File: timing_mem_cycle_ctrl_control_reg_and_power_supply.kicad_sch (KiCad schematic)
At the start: 59 parts, among them U10 LS175, U11 LS20, U20 LS10, U21 LS161, U30 LS20, U31 LS00, U32 LS109, U4 LS04, U42 LS109, U5 LS109, U50 LS368, U52 LS00, U57 LS13, U60 7406, U62 LS08

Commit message: First version of the schematic completed
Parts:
- U10: symbol 74LS175:74LS175_U10 -> LS_Logic:74LS175_U10
- U11: symbol 74LS20:74LS20_U11 -> LS_Logic:74LS20_U11
- U20: symbol 74LS10:74LS10_U20 -> LS_Logic:74LS10_U20
- U21: symbol 74LS161:74LS161_U21 -> LS_Logic:74LS161_U21
- U4: footprint Package_DIP:DIP-14_W7.62mm_LongPads -> (none)
- U50: symbol 74LS368:74LS368_U50 -> LS_Logic:74LS368_U50_U59
- U57: symbol 74xx:74LS13 -> LS_Logic:74LS13_U57
- renumbered C1000 to C101
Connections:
- net +5V: now also VR2.3 (OUT); no longer VR2.1 (IN)
- net 6502_+7.5V: now also VR2.1 (IN); no longer VR2.3 (OUT)
- net CNTC: no longer JP1.3 (C), U11.9, U21.11 (Q3), U5.12 (C)
- net MEM_CYC_ENAB renamed MEM_CYC_ENABLE
- net SYST_RAM_ADDR renamed SYST_RAM_ADRD
- net USR_RAM_ADDR renamed USER_RAM_ADRD
- net ~{MEM_MODE} renamed ~{MFM_MODE}
- new net: JP1.3 (C), U11.9, U21.11 (Q3), U5.12 (C)
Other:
- moved on the sheet: VR2

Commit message: Schematic corrections
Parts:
- C10, C11, C8: footprint (none) -> K_1013_Jumper:CP_Radial_D8.0mm_P5.08mm
- C7: footprint (none) -> K_1013_Jumper:CP_Axial_L30.0mm_D12.5mm_P36.83mm_Horizontal
- C88, C89, C9, C98, C99: footprint (none) -> K_1013_Jumper:C_Disc_D7.0mm_W2.5mm_P6.35mm
- D1, D2, D3: footprint (none) -> K_1013_Jumper:D_DO-35_SOD27_P12.70mm_Horizontal
- R11: footprint Resistor_THT:R_Axial_DIN0207_L6.3mm_D2.5mm_P10.16mm_Horizontal -> K_1013_Jumper:R_Axial_DIN0309_L9.0mm_D3.2mm_P12.70mm_Horizontal
- R11: footprint Resistor_THT:R_Axial_DIN0207_L6.3mm_D2.5mm_P10.16mm_Horizontal -> K_1013_Jumper:R_Axial_DIN0204_L3.6mm_D2.5mm_P12.70mm_Horizontal
- R27: footprint (none) -> K_1013_Jumper:Potentiometer_Bourns_3339P_Vertical
- TP1: footprint (none) -> K_1013_Jumper:TestPoint_1.8
- TP11, TP13, TP5, TP6: footprint (none) -> K_1013_Jumper:TestPoint
- TP2: footprint (none) -> K_1013_Jumper:TestPoint_2.4
- TP3, TP7: footprint (none) -> K_1013_Jumper:TestPoint_3.0
- U10, U21, U32, U42, U5, U50: footprint (none) -> K_1013_Jumper:DIP-16_W7.62mm_LongPads
- U11, U30, U4: footprint Package_DIP:DIP-14_W7.62mm_LongPads -> K_1013_Jumper:DIP-14_W7.62mm_LongPads
- U20, U31, U4, U52, U57, U60, U62: footprint (none) -> K_1013_Jumper:DIP-14_W7.62mm_LongPads
- VR1: footprint (none) -> K_1013_Jumper:TO-202-3_Horizontal_TabDown
- VR2: footprint (none) -> K_1013_Jumper:TO-220-3_Horizontal_TabDown

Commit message: Update progress
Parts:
- C10, C11, C8: footprint K_1013_Jumper:CP_Radial_D8.0mm_P5.08mm -> K_1013:CP_Radial_D8.0mm_P5.08mm
- C7: footprint K_1013_Jumper:CP_Axial_L30.0mm_D12.5mm_P36.83mm_Horizontal -> K_1013:CP_Axial_L30.0mm_D12.5mm_P35.56mm_Horizontal
- C88, C89, C9, C98, C99: footprint K_1013_Jumper:C_Disc_D7.0mm_W2.5mm_P6.35mm -> K_1013:C_Disc_D7.0mm_W2.5mm_P6.35mm
- D1, D2, D3: footprint K_1013_Jumper:D_DO-35_SOD27_P12.70mm_Horizontal -> K_1013:D_DO-35_SOD27_P12.70mm_Horizontal
- JP1: footprint K_1013_Jumper:Jumper-4 -> K_1013:Jumper-4
- R13, R14, R5, R6: renamed from R11; footprint K_1013_Jumper:R_Axial_DIN0204_L3.6mm_D2.5mm_P12.70mm_Horizontal -> K_1013:R_Axial_DIN0204_L3.6mm_D2.5mm_P12.70mm_Horizontal
- R22, R28, R29, R30, R31, R53, R54, R55: renamed from R11; footprint K_1013_Jumper:R_Axial_DIN0309_L9.0mm_D3.2mm_P12.70mm_Horizontal -> K_1013:R_Axial_DIN0309_L9.0mm_D3.2mm_P12.70mm_Horizontal
- R27: footprint K_1013_Jumper:Potentiometer_Bourns_3339P_Vertical -> K_1013:Potentiometer_Bourns_3339P_Vertical
- TP1: footprint K_1013_Jumper:TestPoint_1.8 -> K_1013:TestPoint_1.8
- TP11, TP13, TP5, TP6: footprint K_1013_Jumper:TestPoint -> K_1013:TestPoint
- TP2: footprint K_1013_Jumper:TestPoint_2.4 -> K_1013:TestPoint_2.4
- TP3, TP7: footprint K_1013_Jumper:TestPoint_3.0 -> K_1013:TestPoint_3.0
- U10, U21, U32, U42, U5, U50: footprint K_1013_Jumper:DIP-16_W7.62mm_LongPads -> K_1013:DIP-16_W7.62mm_LongPads
- U11, U20, U30, U31, U4, U52, U57, U60, U62: footprint K_1013_Jumper:DIP-14_W7.62mm_LongPads -> K_1013:DIP-14_W7.62mm_LongPads
- U19: renamed from U4; footprint K_1013_Jumper:DIP-14_W7.62mm_LongPads -> K_1013:DIP-14_W7.62mm_LongPads_U19
- U51, U53: renamed from U4; footprint K_1013_Jumper:DIP-14_W7.62mm_LongPads -> K_1013:DIP-14_W7.62mm_LongPads
- VR1: footprint K_1013_Jumper:TO-202-3_Horizontal_TabDown -> K_1013:TO-202-3_Horizontal_TabDown
- VR2: footprint K_1013_Jumper:TO-220-3_Horizontal_TabDown -> K_1013:TO-220-3_Horizontal_TabDown
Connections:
- net 6502_+7.5V: now also C11.1; no longer C11.2
- net 6502_Ø2: now also U4.5; no longer U4.1
- net 8MHZ_CLOCK: now also U51.4; no longer U51.2
- net CNTB: now also U4.9; no longer U4.1
- net DMA_CYC: now also U53.12; no longer U53.2
- net FDC_WRT_CLK: now also U4.12; no longer U4.2
- net GND: now also C11.2; no longer C11.1
- net LOC_~{R}/W: now also U30.2; no longer U30.10
- net LOC_Ø2: now also U19.12; no longer U19.2
- net REF_CYC: now also U4.10; no longer U4.2
- net SYST_RAM_ADRD: now also U30.1; no longer U30.9
- net ~{CNTC}: now also U30.4; no longer U30.12
- net ~{DMA_CYC}: now also U53.13; no longer U53.1
- net ~{LOC_Ø2}: now also U19.13, U4.6; no longer U19.1, U4.2
- net ~{REF_CYC}: now also U4.11; no longer U4.1
- net at U20.10, U31.5: now also U4.8; no longer U4.2
- net at R27.2, R27.3, U21.2 (CP)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: now also U51.3; no longer U51.1
- net at U11.6: now also U4.13; no longer U4.1
- net at U10.6 (~{Q1}): now also U30.5; no longer U30.13
- net at U20.13: now also U30.6; no longer U30.8
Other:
- moved on the sheet: C11

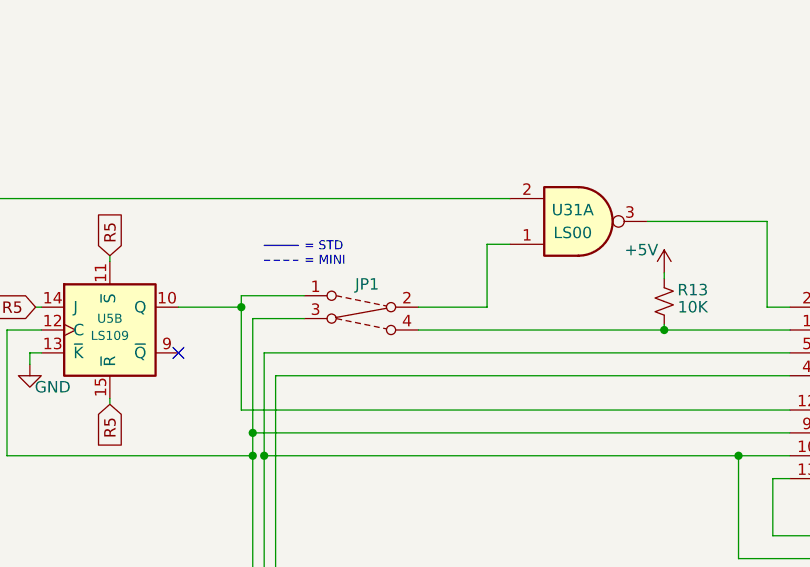
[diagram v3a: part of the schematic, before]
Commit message: Routing of the bottom layer completed
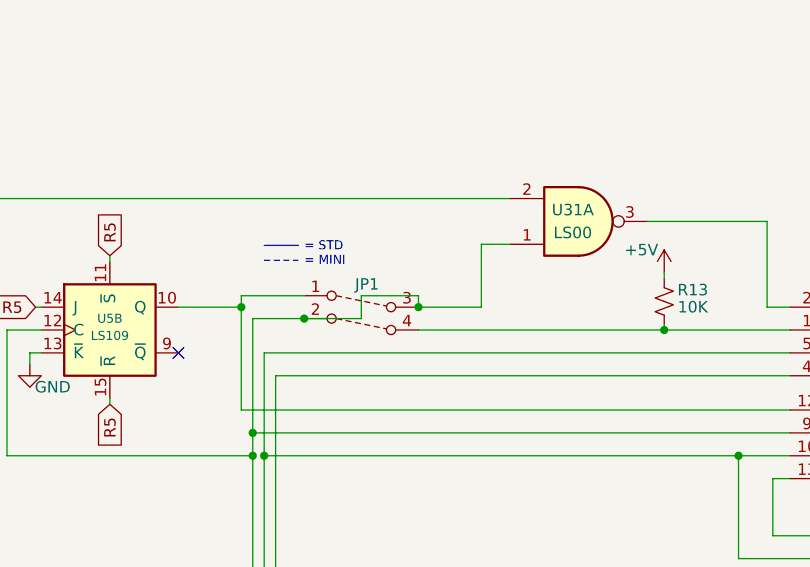
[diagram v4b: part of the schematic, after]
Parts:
- U21: footprint K_1013:DIP-16_W7.62mm_LongPads -> K_1013:DIP-16_W7.62mm_LongPads_U21
- U30: footprint K_1013:DIP-14_W7.62mm_LongPads -> K_1013:DIP-14_W7.62mm_LongPads_U30
- U31: footprint K_1013:DIP-14_W7.62mm_LongPads -> K_1013:DIP-14_W7.62mm_LongPads_U31
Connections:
- net at JP1.3, U11.9, U21.11 (Q3)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: now also JP1.2, U31.1
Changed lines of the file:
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@@
   (junction (at 341.63 210.185) (diameter 0) (color 0 0 0 0)
   )
+  (junction (at 86.995 59.69) (diameter 0) (color 0 0 0 0)
+  )
   (junction (at 80.645 200.025) (diameter 0) (color 0 0 0 0)
   )
@@
   (junction (at 351.79 151.765) (diameter 0) (color 0 0 0 0)
   )
+  (junction (at 81.28 74.93) (diameter 0) (color 0 0 0 0)
+  )
   (junction (at 369.57 160.655) (diameter 0) (color 0 0 0 0)
   )
@@
   (junction (at 235.585 86.36) (diameter 0) (color 0 0 0 0)
   )
-  (junction (at 81.28 72.39) (diameter 0) (color 0 0 0 0)
-  )
   (junction (at 370.205 198.12) (diameter 0) (color 0 0 0 0)
   )
@@
   (junction (at 280.67 97.155) (diameter 0) (color 0 0 0 0)
   )
-  (junction (at 81.28 74.93) (diameter 0) (color 0 0 0 0)
-  )
   (junction (at 341.63 198.12) (diameter 0) (color 0 0 0 0)
   )
@@
   (junction (at 299.72 198.12) (diameter 0) (color 0 0 0 0)
   )
+  (junction (at 81.28 72.39) (diameter 0) (color 0 0 0 0)
+  )
   (junction (at 321.31 210.185) (diameter 0) (color 0 0 0 0)
   )
@@
   (junction (at 370.205 210.185) (diameter 0) (color 0 0 0 0)
   )
+  (junction (at 99.695 58.42) (diameter 0) (color 0 0 0 0)
+  )
   (junction (at 302.895 123.19) (diameter 0) (color 0 0 0 0)
   )
@@
     (stroke (width 0) (type default))
   )
+  (wire (pts (xy 81.28 72.39) (xy 140.97 72.39))
+    (stroke (width 0) (type default))
+  )
   (wire (pts (xy 47.625 142.24) (xy 47.625 144.78))
     (stroke (width 0) (type default))
@@
     (stroke (width 0) (type default))
   )
-  (wire (pts (xy 107.315 58.42) (xy 107.315 51.435))
-    (stroke (width 0) (type default))
-  )
   (wire (pts (xy 302.895 123.19) (xy 382.905 123.19))
     (stroke (width 0) (type default))
@@
     (stroke (width 0) (type default))
   )
+  (wire (pts (xy 81.28 59.69) (xy 81.28 72.39))
+    (stroke (width 0) (type default))
+  )
   (wire (pts (xy 263.525 146.05) (xy 299.72 146.05))
     (stroke (width 0) (type default))
@@
     (stroke (width 0) (type default))
   )
-  (wire (pts (xy 107.315 51.435) (xy 109.855 51.435))
-    (stroke (width 0) (type default))
-  )
-  (wire (pts (xy 81.28 127) (xy 78.105 127))
-    (stroke (width 0) (type default))
-  )
   (wire (pts (xy 162.56 107.95) (xy 154.305 107.95))
     (stroke (width 0) (type default))
@@
     (stroke (width 0) (type default))
   )
+  (wire (pts (xy 99.695 57.15) (xy 99.695 58.42))
+    (stroke (width 0) (type default))
+  )
   (wire (pts (xy 275.59 83.82) (xy 276.86 83.82))
     (stroke (width 0) (type default))
@@
     (stroke (width 0) (type default))
   )
+  (wire (pts (xy 81.28 72.39) (xy 81.28 74.93))
+    (stroke (width 0) (type default))
+  )
   (wire (pts (xy 107.95 120.015) (xy 136.525 120.015))
     (stroke (width 0) (type default))
@@
     (stroke (width 0) (type default))
   )
-  (wire (pts (xy 53.975 74.93) (xy 81.28 74.93))
-    (stroke (width 0) (type default))
-  )
   (wire (pts (xy 260.35 88.9) (xy 257.81 88.9))
     (stroke (width 0) (type default))
@@
     (stroke (width 0) (type default))
   )
+  (wire (pts (xy 86.995 59.69) (xy 93.345 59.69))
+    (stroke (width 0) (type default))
+  )
   (wire (pts (xy 328.93 222.25) (xy 341.63 222.25))
     (stroke (width 0) (type default))
@@
     (stroke (width 0) (type default))
   )
-  (wire (pts (xy 81.28 72.39) (xy 140.97 72.39))
+  (wire (pts (xy 93.345 57.15) (xy 99.695 57.15))
+    (stroke (width 0) (type default))
+  )
+  (wire (pts (xy 53.975 74.93) (xy 81.28 74.93))
     (stroke (width 0) (type default))
   )
@@
     (stroke (width 0) (type default))
   )
-  (wire (pts (xy 109.855 113.665) (xy 107.95 113.665))
+  (wire (pts (xy 99.695 58.42) (xy 106.68 58.42))
     (stroke (width 0) (type default))
   )
-  (wire (pts (xy 81.28 74.93) (xy 81.28 127))
+  (wire (pts (xy 109.855 113.665) (xy 107.95 113.665))
     (stroke (width 0) (type default))
   )
@@
     (stroke (width 0) (type default))
   )
+  (wire (pts (xy 81.28 74.93) (xy 81.28 127))
+    (stroke (width 0) (type default))
+  )
   (wire (pts (xy 57.15 58.42) (xy 57.785 58.42))
     (stroke (width 0) (type default))
@@
     (stroke (width 0) (type default))
   )
-  (wire (pts (xy 81.28 72.39) (xy 81.28 74.93))
-    (stroke (width 0) (type default))
-  )
   (wire (pts (xy 304.8 62.865) (xy 304.8 74.93))
     (stroke (width 0) (type default))
@@
     (stroke (width 0) (type default))
   )
+  (wire (pts (xy 106.68 51.435) (xy 106.68 58.42))
+    (stroke (width 0) (type default))
+  )
+  (wire (pts (xy 81.28 127) (xy 78.105 127))
+    (stroke (width 0) (type default))
+  )
   (wire (pts (xy 133.985 160.02) (xy 133.985 189.23))
     (stroke (width 0) (type default))
@@
     (stroke (width 0) (type default))
   )
-  (wire (pts (xy 99.695 58.42) (xy 107.315 58.42))
-    (stroke (width 0) (type default))
-  )
   (wire (pts (xy 106.045 207.645) (xy 111.125 207.645))
     (stroke (width 0) (type default))
@@
     (stroke (width 0) (type default))
   )
+  (wire (pts (xy 86.995 59.69) (xy 81.28 59.69))
+    (stroke (width 0) (type default))
+  )
   (wire (pts (xy 379.73 198.12) (xy 382.905 198.12))
     (stroke (width 0) (type default))
@@
     (stroke (width 0) (type default))
   )
-  (wire (pts (xy 86.995 59.69) (xy 81.28 59.69))
-    (stroke (width 0) (type default))
-  )
   (wire (pts (xy 140.97 63.5) (xy 82.55 63.5))
     (stroke (width 0) (type default))
@@
     (stroke (width 0) (type default))
   )
+  (wire (pts (xy 109.855 51.435) (xy 106.68 51.435))
+    (stroke (width 0) (type default))
+  )
   (wire (pts (xy 83.82 90.805) (xy 83.82 98.425))
     (stroke (width 0) (type default))
@@
     (stroke (width 0) (type default))
   )
+  (wire (pts (xy 93.345 59.69) (xy 93.345 57.15))
+    (stroke (width 0) (type default))
+  )
   (wire (pts (xy 368.935 53.34) (xy 382.905 53.34))
     (stroke (width 0) (type default))
@@
     (stroke (width 0) (type default))
   )
-  (wire (pts (xy 81.28 59.69) (xy 81.28 72.39))
-    (stroke (width 0) (type default))
-  )
   (wire (pts (xy 176.53 62.23) (xy 186.69 62.23))
     (stroke (width 0) (type default))
@@
       (effects (font (size 1.27 1.27)))
     )
-    (property "Footprint" "K_1013:DIP-16_W7.62mm_LongPads" (at 65.405 139.7 0)
+    (property "Footprint" "K_1013:DIP-16_W7.62mm_LongPads_U21" (at 65.405 139.7 0)
       (effects (font (size 1.27 1.27)) hide)
     )
@@
       (effects (font (size 1.27 1.27)))
     )
-    (property "Footprint" "K_1013:DIP-14_W7.62mm_LongPads" (at 360.68 117.475 0)
+    (property "Footprint" "K_1013:DIP-14_W7.62mm_LongPads_U31" (at 360.68 117.475 0)
       (effects (font (size 1.27 1.27)) hide)
     )
@@
       (effects (font (size 1.27 1.27)))
     )
-    (property "Footprint" "K_1013:DIP-14_W7.62mm_LongPads" (at 316.865 104.14 0)
+    (property "Footprint" "K_1013:DIP-14_W7.62mm_LongPads_U30" (at 316.865 104.14 0)
       (effects (font (size 1.27 1.27)) hide)
     )
@@
       (effects (font (size 1.27 1.27)))
     )
-    (property "Footprint" "K_1013:DIP-14_W7.62mm_LongPads" (at 117.475 48.895 0)
+    (property "Footprint" "K_1013:DIP-14_W7.62mm_LongPads_U31" (at 117.475 48.895 0)
       (effects (font (size 1.27 1.27)) hide)
     )
@@
       (effects (font (size 1.27 1.27)))
     )
-    (property "Footprint" "K_1013:DIP-14_W7.62mm_LongPads" (at 65.405 172.72 0)
+    (property "Footprint" "K_1013:DIP-14_W7.62mm_LongPads_U31" (at 65.405 172.72 0)
       (effects (font (size 1.27 1.27)) hide)
     )
@@
       (effects (font (size 1.27 1.27)))
     )
-    (property "Footprint" "K_1013:DIP-14_W7.62mm_LongPads" (at 117.475 111.125 0)
+    (property "Footprint" "K_1013:DIP-14_W7.62mm_LongPads_U31" (at 117.475 111.125 0)
       (effects (font (size 1.27 1.27)) hide)
     )
